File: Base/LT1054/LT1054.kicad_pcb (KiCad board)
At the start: 2 copper layers, 30 x 84 mm, 41 parts, among them J1 Barrel_Jack_Switch, J2 Ground, J3 Conn_01x03_Pin, J4 Conn_01x03_Pin, J5 AudioJack2_Ground, J6 AudioJack2_Ground, Q1 BC846, Q2 40V, U1 LT1054, U2 OPA1656

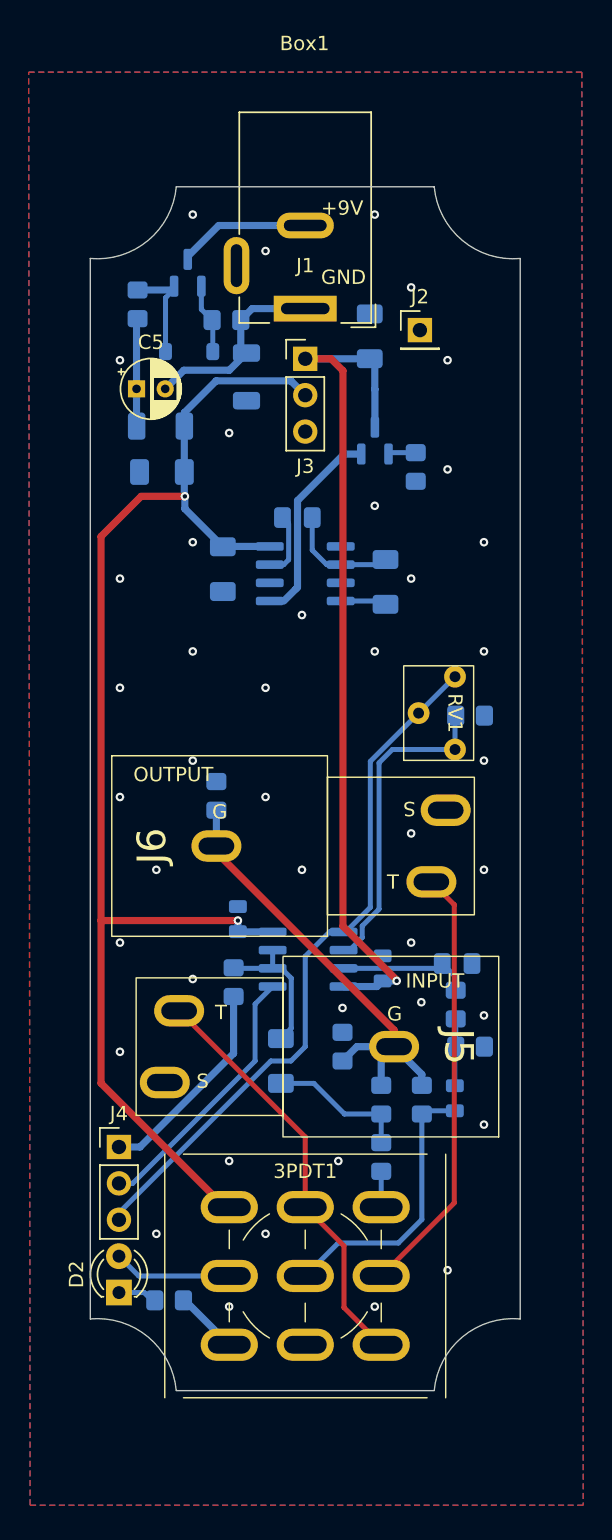
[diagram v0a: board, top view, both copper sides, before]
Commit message: Add back the BUF634A to the audio output
With the dual rails, we don't need to have the output capacitor to
rebase the signal levels, and can drive it directly.  Which allows going
back to the headphone amplifier setup using the BUF634A.

Is this a good idea? I dunno.  Having a separate headphone amplifier
makes more sense, I guess, but I liked just being able to connect the
headphones to test things out.

And it's not like these boards make sense for anybody else anyway, so...

Signed-off-by: Linus Torvalds <torvalds@linux-foundation.org>
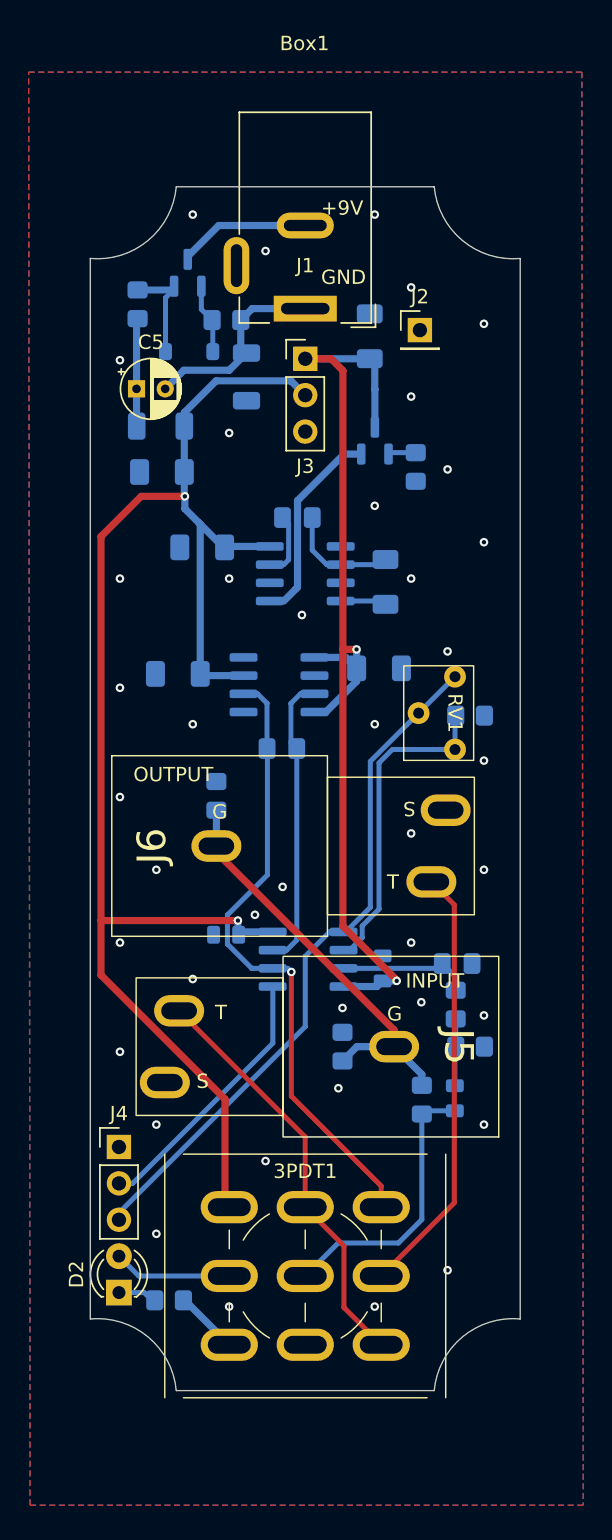
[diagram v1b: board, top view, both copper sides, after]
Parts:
- removed the C11 at (98.3, 119.0)
- removed the R7 at (105.3, 125.7)
- removed the R8 at (95.0, 113.5)
- removed the R9 at (105.3, 121.7)
- added C10: 10uF, Capacitor_SMD:C_1206_3216Metric_Pad1.33x1.80mm_HandSolder, B.Cu at (91.1, 92.0)
- added C13: 10pF, Capacitor_SMD:C_0805_2012Metric_Pad1.18x1.45mm_HandSolder, B.Cu at (98.4, 97.2)
- added C9: 10uF, Capacitor_SMD:C_1206_3216Metric_Pad1.33x1.80mm_HandSolder, B.Cu at (105.2, 91.6)
- added U3: BUF634AxD, Package_SO:SOIC-8_3.9x4.9mm_P1.27mm, B.Cu at (98.2, 92.7)
- moved C1 2.09 mm to (92.8, 83.2), turned to 180 degrees
- moved C12 1.36 mm to (94.5, 110.2), turned to 180 degrees
- renumbered C9 to C11, C10 to C12, R13 to R10, R10 to R7, R11 to R8, R12 to R9
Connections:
- U2 pad 6: Net-(U2B--) -> OUT^{RAW}
- U2 pad 7: Net-(U2B--) -> Net-(U2B-OUT)
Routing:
- net OUT^{RAW}: track 2.50 -> 44.2 mm, vias 0 -> 1
- net Net-(U2B-OUT): track 0.00 -> 20.0 mm
- net GND: track 18.9 -> 4.24 mm, vias 42 -> 41
- net VIN: track 93.7 -> 107.1 mm
- net Net-(C11-Pad1): track 9.89 -> 0.00 mm
- net -V: track 60.4 -> 70.1 mm, vias 1 -> 2
- net Net-(U2B--): track 9.45 -> 0.00 mm
- net GNDS: track 31.8 -> 28.7 mm
- net IN^{EFF}: track 49.3 -> 48.3 mm
